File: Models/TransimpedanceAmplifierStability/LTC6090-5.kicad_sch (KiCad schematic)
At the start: 20 parts

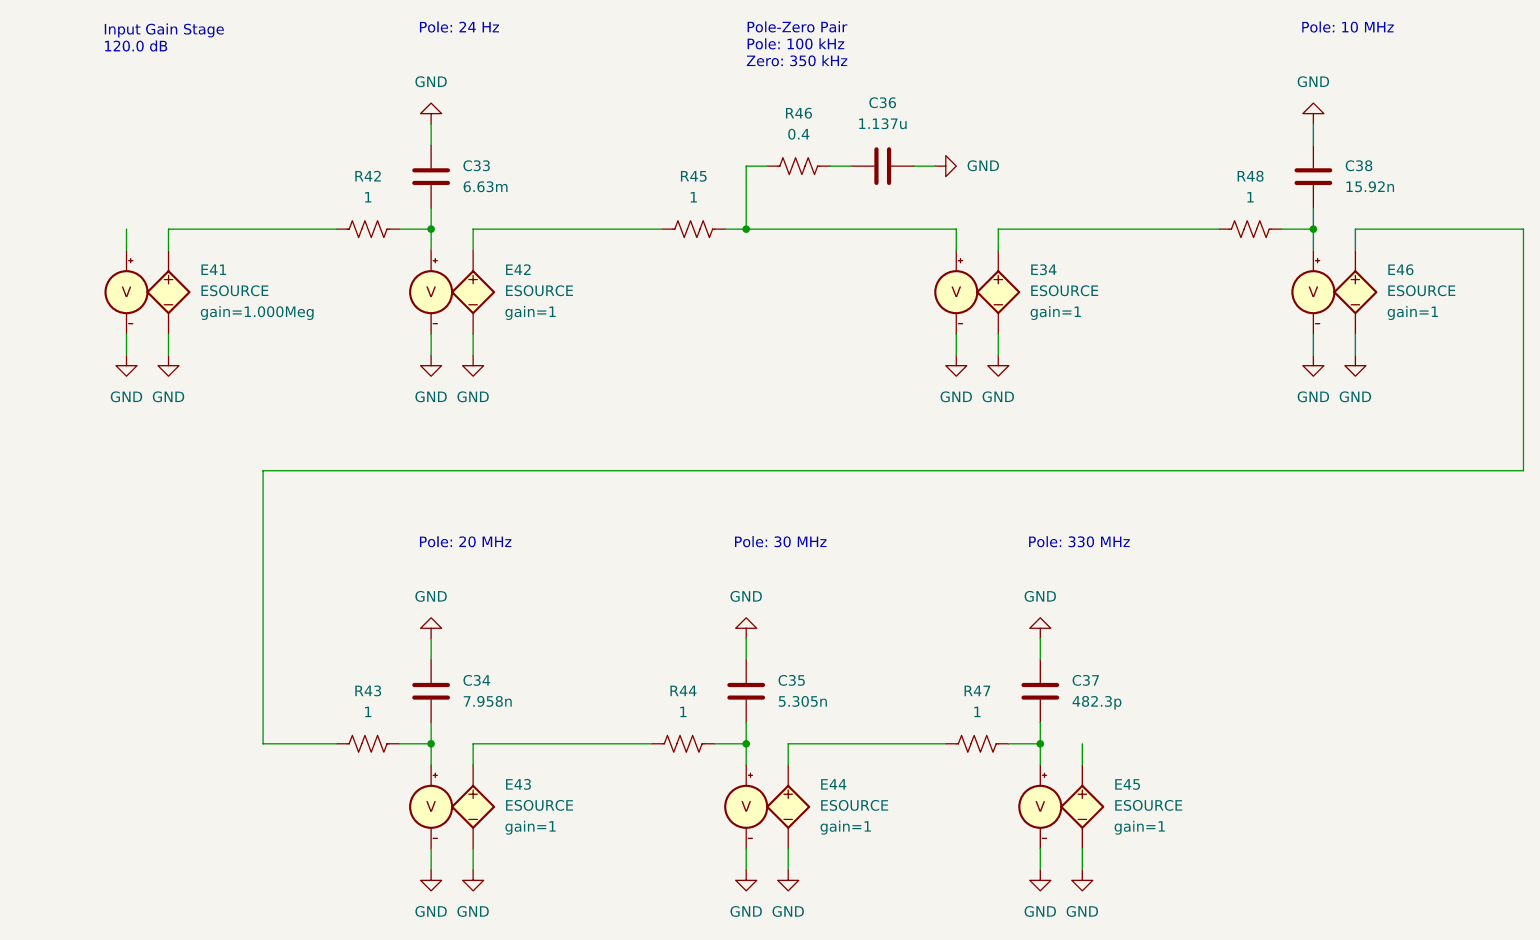
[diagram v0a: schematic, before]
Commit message: Upload latest version of TIA stability KiCad project
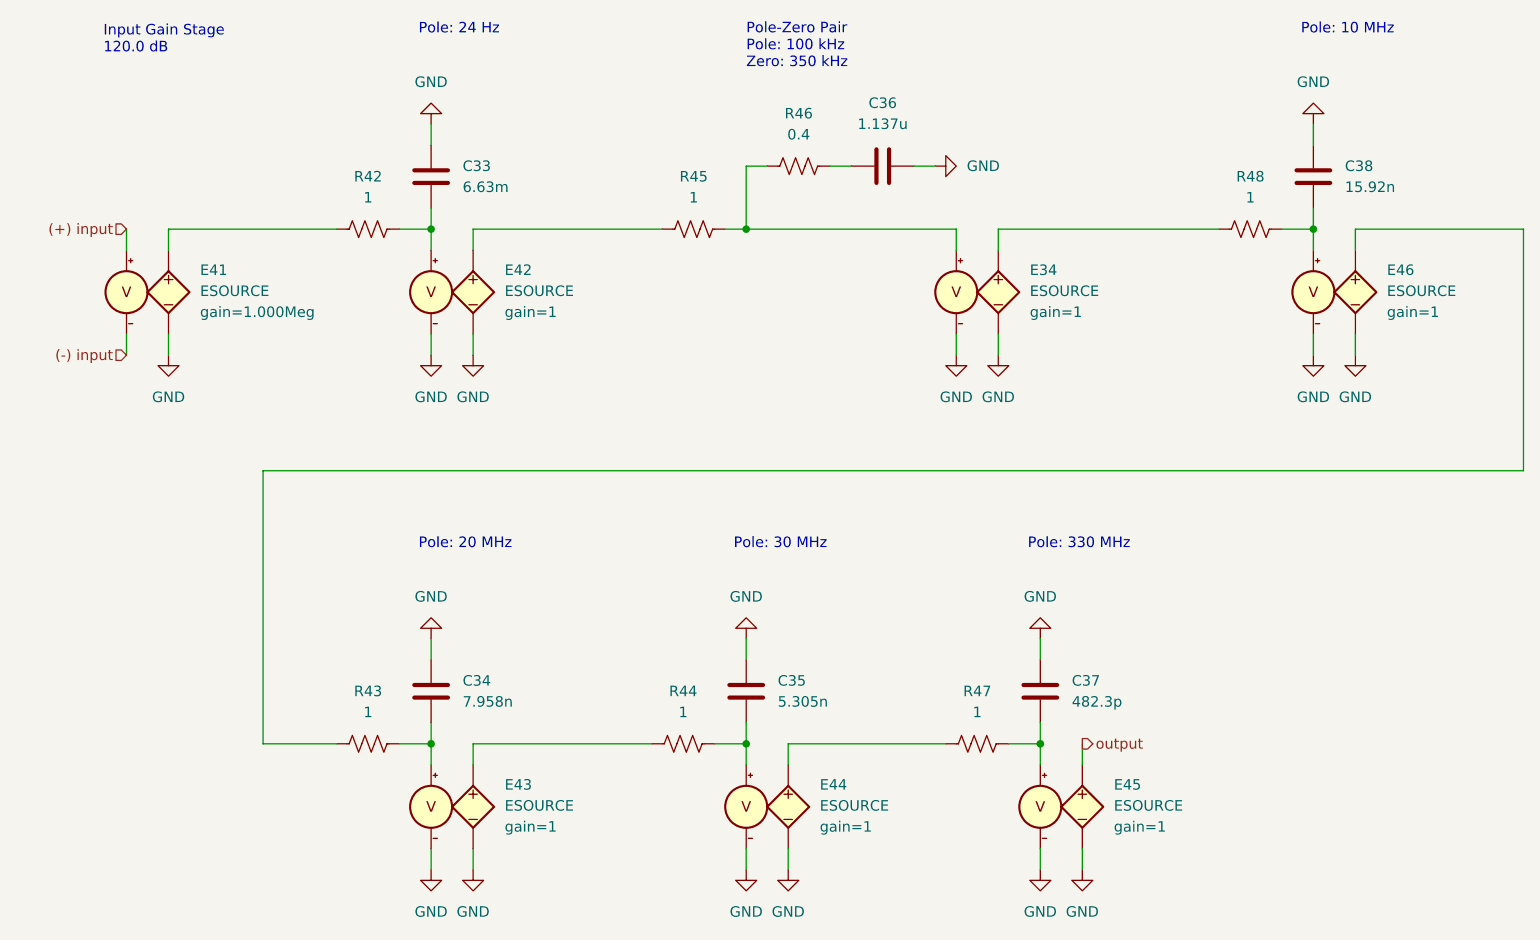
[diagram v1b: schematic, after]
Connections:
- net GND: no longer E41.4 (C-)
- net (+) input: now reaches E41.3 (C+)
- net output: now reaches E45.1 (N+)
- new net (-) input: E41.4 (C-)
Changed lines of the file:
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@@
+		)
+	)
+	(hierarchical_label "(-) input"
+		(shape input)
+		(at 71.12 71.12 180)
+		(effects
+			(font
+				(size 1.27 1.27)
+			)
+			(justify right)
+		)
+	)
+	(hierarchical_label "output"
+		(shape output)
+		(at 186.69 118.11 0)
+		(effects
+			(font
+				(size 1.27 1.27)
+			)
+			(justify left)
+		)
+	)
+	(hierarchical_label "(+) input"
+		(shape input)
+		(at 71.12 55.88 180)
+		(effects
+			(font
+				(size 1.27 1.27)
+			)
+			(justify right)
 		)
 	)
@@
 					(unit 1)
 				)
-			)
-		)
-	)
-	(symbol
-		(lib_id "power:GND")
-		(at 71.12 71.12 0)
-		(unit 1)
-		(exclude_from_sim no)
-		(in_bom yes)
-		(on_board yes)
-		(dnp no)
-		(fields_autoplaced yes)
-		(property "Reference" "#PWR0111"
-			(at 71.12 77.47 0)
-			(effects
-				(font
-					(size 1.27 1.27)
-				)
-				(hide yes)
-			)
-		)
-		(property "Value" "GND"
-			(at 71.12 76.2 0)
-			(effects
-				(font
-					(size 1.27 1.27)
-				)
-			)
-		)
-		(property "Footprint" ""
-			(at 71.12 71.12 0)
-			(effects
-				(font
-					(size 1.27 1.27)
-				)
-				(hide yes)
-			)
-		)
-		(property "Datasheet" ""
-			(at 71.12 71.12 0)
-			(effects
-				(font
-					(size 1.27 1.27)
-				)
-				(hide yes)
-			)
-		)
-		(property "Description" "Power symbol creates a global label with name \"GND\" , ground"
-			(at 71.12 71.12 0)
-			(effects
-				(font
-					(size 1.27 1.27)
-				)
-				(hide yes)
-			)
-		)
-		(pin "1"
-		)
-		(instances
-			(project "TransimpedanceAmplifierStability"
-				(path "/b282eeea-1083-4bd9-aef5-c78f2e129a69/6cbaf1f0-e0d1-4fda-8609-fd183723e12d"
-					(reference "#PWR0111")
-					(unit 1)
-				)
